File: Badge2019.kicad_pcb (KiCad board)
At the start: 2 copper layers, 77.6 x 99 mm, 39 parts, among them SW1 SW_SPDT, U1 ATtiny13A-SU, U2 74164

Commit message: Actual version send for mass production
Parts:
- added ?: , Symbols:WEEE-Logo_4.2x6mm_SilkScreen, B.Cu at (188.8, 85.2)
- R2, R3, R4, R5: footprint OPL_Resistor:R0603 -> Resistors_SMD:R_0603_HandSoldering
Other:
- board text added: "Hacker Lab"
- board text added: "V3 2019"

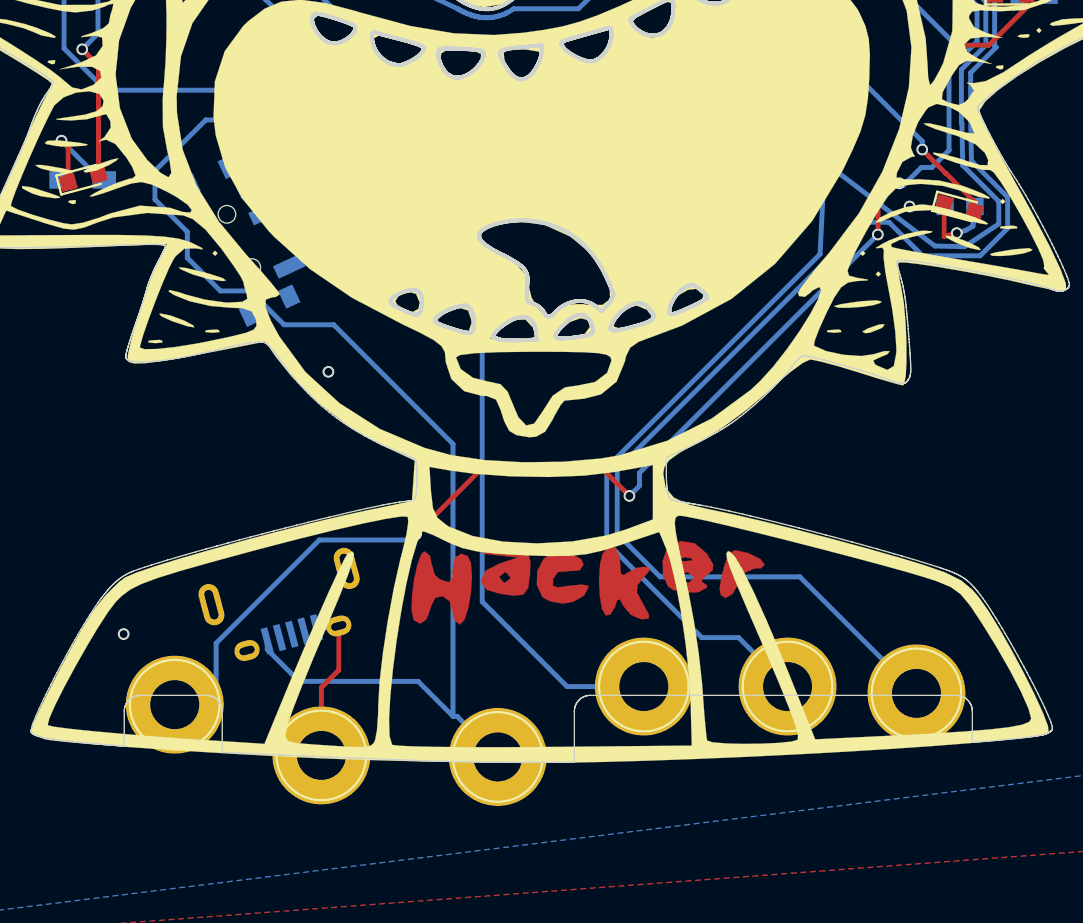
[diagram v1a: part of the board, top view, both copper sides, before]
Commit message: Moved border contacts to be inside the board. created files for jlpcb
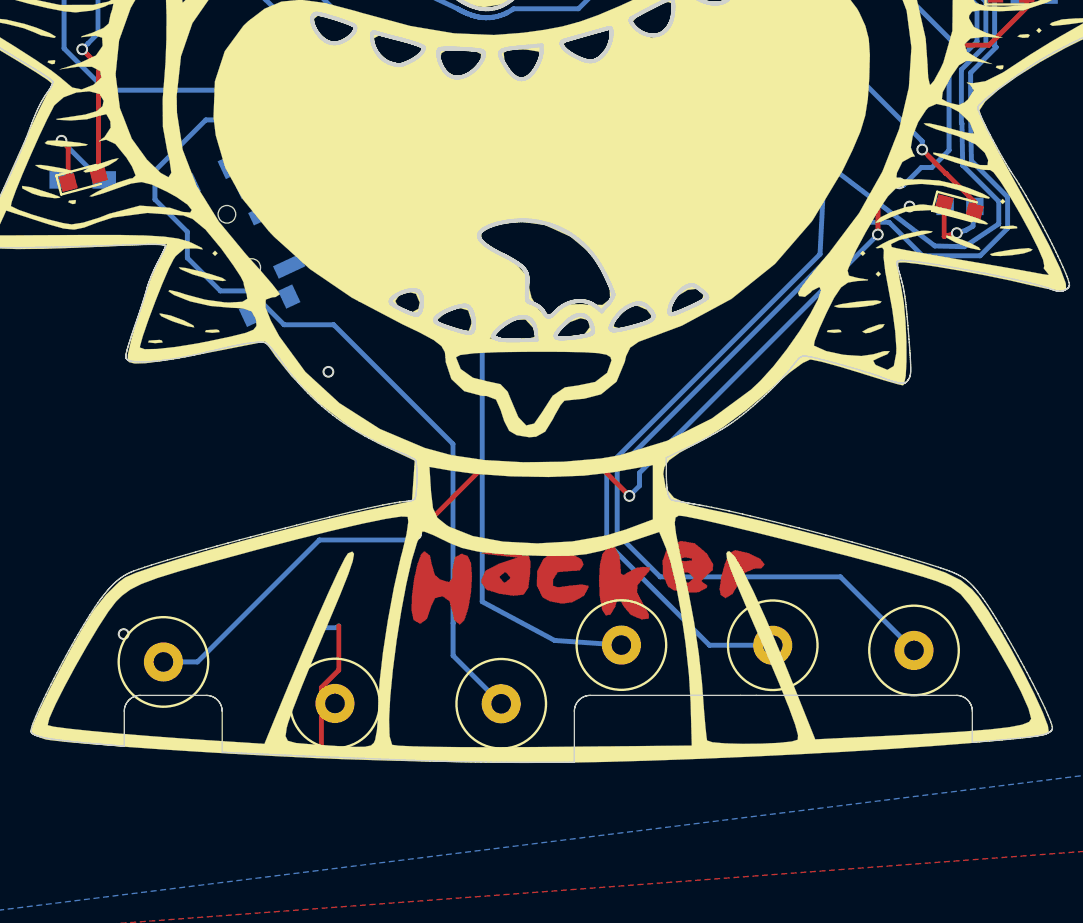
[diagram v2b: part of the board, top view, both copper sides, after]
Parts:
- removed the REF** at (214.9, 136.0)
- removed the REF** at (222.2, 136.0)
- removed the REF** at (198.4, 139.5)
- removed the REF** at (207.4, 139.6)
- removed USB1: MICRO-USB-SMD_ZX62-B-5PA_, OPL_Connector:MICRO-USB5+6P-SMD-0.65-AB
- added REF**: 1pin, Connectors:1pin, F.Cu at (213.7, 133.9)
- added REF**: 1pin, Connectors:1pin, F.Cu at (221.4, 133.9)
- added REF**: 1pin, Connectors:1pin, F.Cu at (199.1, 136.8)
- added REF**: 1pin, Connectors:1pin, F.Cu at (207.6, 136.9)
- moved REF** 2.26 mm to (190.3, 134.7)
- moved REF** 2.20 mm to (228.7, 134.1)
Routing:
- net /VIN5V: track 59.7 -> 45.7 mm
- net /SCK: track 94.1 -> 91.6 mm
- net /MISO: track 133.2 -> 131.6 mm
- net /MOSI: track 129.8 -> 129.1 mm
- net /RST: track 87.8 -> 88.4 mm
